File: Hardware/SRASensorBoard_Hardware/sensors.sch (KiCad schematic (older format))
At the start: 61 parts, among them J1 USB_A, Q1 BSS138, Q2 BSS138, Q3 BSS138, Q4 BSS138, Q5 BSS138, Q6 BSS138, U4 FT230XS

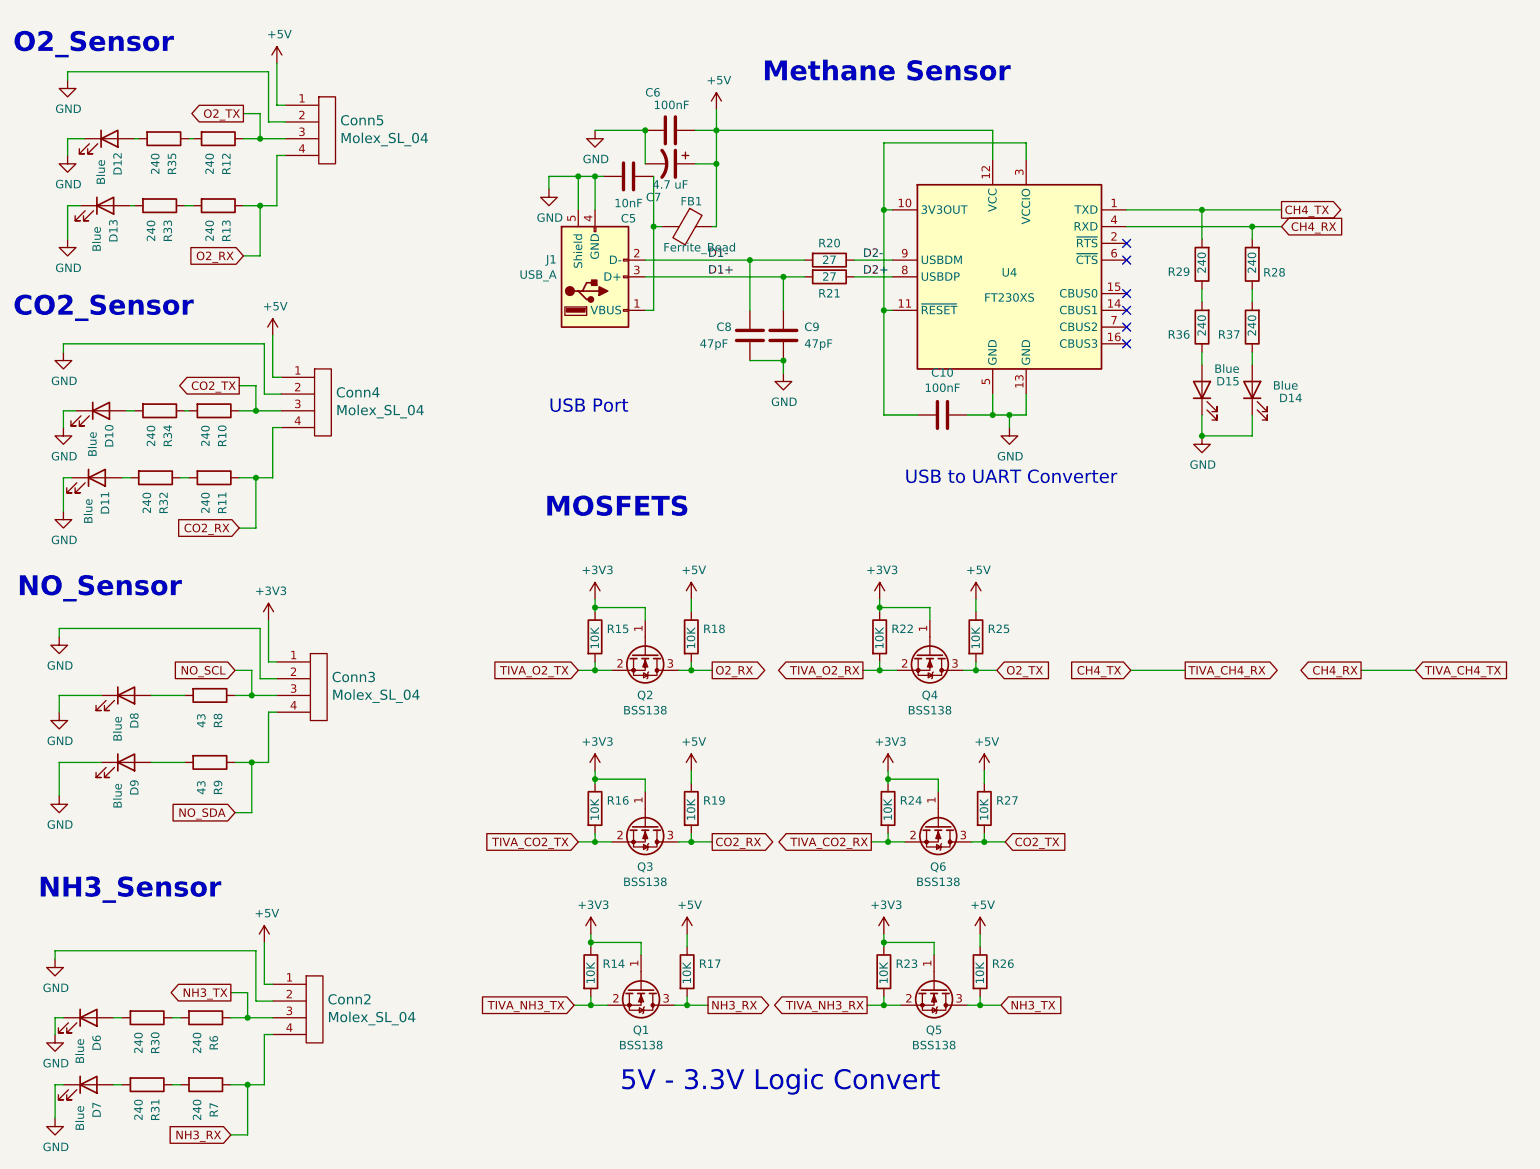
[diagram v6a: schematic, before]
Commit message: Science CDR changes
Changed NO to NO2, removed NH3 data lines for analog output and changed power to 5v, added 3 laser and photodiode pairs (mosfet not determined), added uv and lights connectors, updated tiva pins
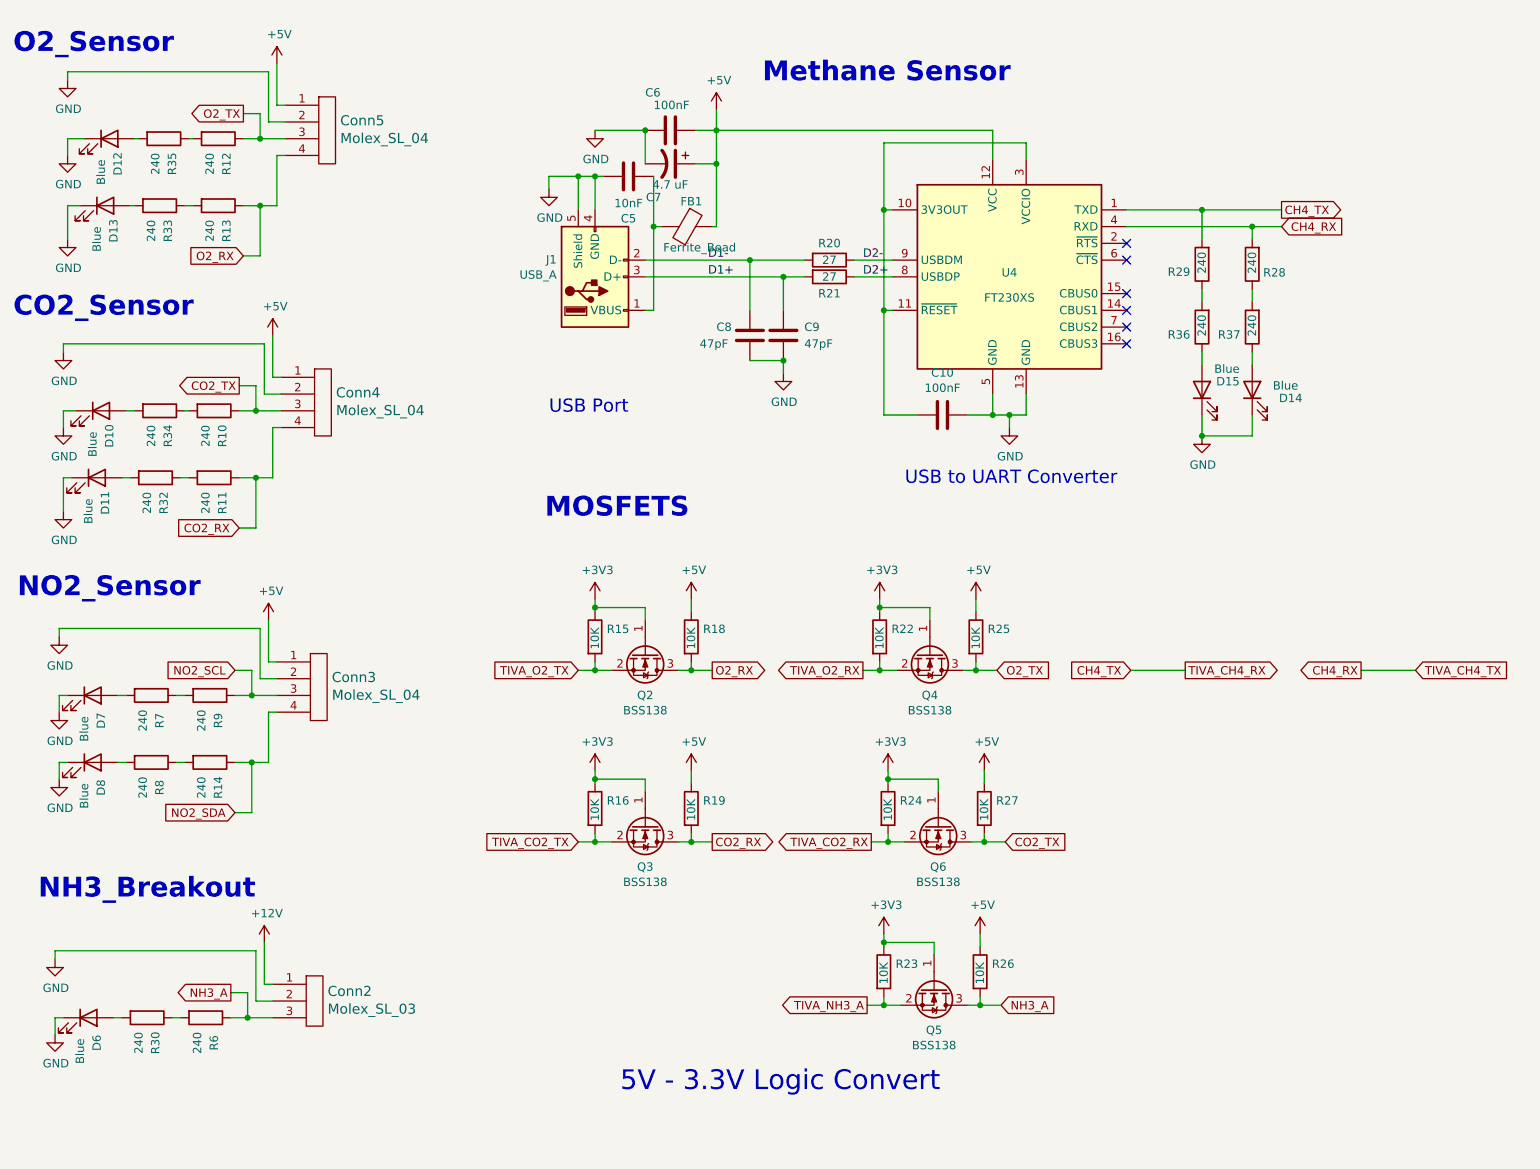
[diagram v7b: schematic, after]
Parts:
- removed Conn2: Molex_SL_04, MRDT_Connectors:MOLEX_SL_04_Horizontal, symbol MRDT_Connectors:Molex_SL_04
- removed D9: Blue, LED_SMD:LED_0603_1608Metric_Pad1.05x0.95mm_HandSolder, symbol Device:LED
- removed Q1: BSS138, Package_TO_SOT_SMD:SOT-23, symbol Transistor_FET:BSS138
- removed R17: 10K, Resistor_SMD:R_0603_1608Metric_Pad1.05x0.95mm_HandSolder, symbol Device:R
- removed R31: 240, Resistor_SMD:R_0603_1608Metric_Pad1.05x0.95mm_HandSolder, symbol Device:R
- added Conn2: Molex_SL_03, symbol MRDT_Connectors:Molex_SL_03
- R14: value 10K -> 240
- R8, R9: value 43 -> 240
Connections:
- net NH3_RX is gone; now on an unnamed net: R7.1
- net TIVA_NH3_TX is gone; now on an unnamed net: R14.2
- net +3V3: no longer Conn3.1, R14.1
- net +5V: now also Conn3.1
- net GND: now also Conn2.2
- net at R7.2: now also D7.2 (A)
- net NH3_TX renamed NH3_A
- net NH3_A: now also Conn2.3
- net NO_SCL: no longer names the net of R8.1
- net NO_SCL: no longer Conn3.3
- net NO_SDA renamed NO2_SCL
- net NO2_SCL: now also Conn3.3; no longer Conn3.4
- net TIVA_NH3_RX renamed TIVA_NH3_A
- new net +12V: Conn2.1
- new net NO2_SDA: Conn3.4, R14.1
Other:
- note added: "NH3_Breakout"
- note added: "NO2_Sensor"
- note removed: "NH3_Sensor"
- note removed: "NO_Sensor"

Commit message: All changes didn't update
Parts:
- Conn2: footprint (none) -> MRDT_Connectors:MOLEX_SL_03_Horizontal
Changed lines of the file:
@@
 F 0 "Conn2" H 2428 6808 60  0000 L CNN
 F 1 "Molex_SL_03" H 2428 6702 60  0000 L CNN
-F 2 "" H 2300 6600 60  0001 C CNN
+F 2 "MRDT_Connectors:MOLEX_SL_03_Horizontal" H 2300 6600 60  0001 C CNN
 F 3 "" H 2300 6600 60  0001 C CNN
 	1    2300 6600
